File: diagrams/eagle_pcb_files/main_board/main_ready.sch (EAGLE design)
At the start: 32 parts

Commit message: prepare main board for production
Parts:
- C1, C2, C3, C4, C6, C7: value (none) -> 100nF
- FUSE1, FUSE2: value (none) -> 1.5A
- R1, R2: value (none) -> 10k
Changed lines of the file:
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@@
 <part name="RAO3" library="POLOLU-VoltageConverter" deviceset="S7V8F3" device=""/>
 <part name="BAT1" library="pinhead" deviceset="PINHD-1X2" device=""/>
-<part name="FUSE1" library="pinhead" deviceset="PINHD-1X2" device=""/>
+<part name="FUSE1" library="pinhead" deviceset="PINHD-1X2" device="" value="1.5A"/>
 <part name="RAO4" library="POLOLU-VoltageConverter" deviceset="S7V8F3" device=""/>
 <part name="BAT2" library="pinhead" deviceset="PINHD-1X2" device=""/>
-<part name="FUSE2" library="pinhead" deviceset="PINHD-1X2" device=""/>
+<part name="FUSE2" library="pinhead" deviceset="PINHD-1X2" device="" value="1.5A"/>
 <part name="U$3" library="SparFun-FuelGauge" deviceset="POLOLU_FUEL_GAUGE" device="BREAKBOARD"/>
 <part name="U$9" library="SparFun-FuelGauge" deviceset="POLOLU_FUEL_GAUGE" device="BREAKBOARD"/>
-<part name="C1" library="rcl" library_urn="urn:adsk.eagle:library:334" deviceset="C-EU" device="C0402" package3d_urn="urn:adsk.eagle:package:23626/1"/>
-<part name="C2" library="rcl" library_urn="urn:adsk.eagle:library:334" deviceset="C-EU" device="C0402" package3d_urn="urn:adsk.eagle:package:23626/1"/>
-<part name="C3" library="rcl" library_urn="urn:adsk.eagle:library:334" deviceset="C-EU" device="C0402" package3d_urn="urn:adsk.eagle:package:23626/1"/>
-<part name="C6" library="rcl" library_urn="urn:adsk.eagle:library:334" deviceset="C-EU" device="C0402" package3d_urn="urn:adsk.eagle:package:23626/1"/>
-<part name="C7" library="rcl" library_urn="urn:adsk.eagle:library:334" deviceset="C-EU" device="C0402" package3d_urn="urn:adsk.eagle:package:23626/1"/>
+<part name="C1" library="rcl" library_urn="urn:adsk.eagle:library:334" deviceset="C-EU" device="C0402" package3d_urn="urn:adsk.eagle:package:23626/1" value="100nF"/>
+<part name="C2" library="rcl" library_urn="urn:adsk.eagle:library:334" deviceset="C-EU" device="C0402" package3d_urn="urn:adsk.eagle:package:23626/1" value="100nF"/>
+<part name="C3" library="rcl" library_urn="urn:adsk.eagle:library:334" deviceset="C-EU" device="C0402" package3d_urn="urn:adsk.eagle:package:23626/1" value="100nF"/>
+<part name="C6" library="rcl" library_urn="urn:adsk.eagle:library:334" deviceset="C-EU" device="C0402" package3d_urn="urn:adsk.eagle:package:23626/1" value="100nF"/>
+<part name="C7" library="rcl" library_urn="urn:adsk.eagle:library:334" deviceset="C-EU" device="C0402" package3d_urn="urn:adsk.eagle:package:23626/1" value="100nF"/>
 <part name="GND2" library="supply1" library_urn="urn:adsk.eagle:library:371" deviceset="GND" device=""/>
 <part name="GND3" library="supply1" library_urn="urn:adsk.eagle:library:371" deviceset="GND" device=""/>
@@
 <part name="C9" library="rcl" library_urn="urn:adsk.eagle:library:334" deviceset="C-EU" device="C0402" package3d_urn="urn:adsk.eagle:package:23626/1" value="100 nF"/>
 <part name="GND5" library="supply1" library_urn="urn:adsk.eagle:library:371" deviceset="GND" device=""/>
-<part name="C4" library="rcl" library_urn="urn:adsk.eagle:library:334" deviceset="C-EU" device="C0402" package3d_urn="urn:adsk.eagle:package:23626/1"/>
+<part name="C4" library="rcl" library_urn="urn:adsk.eagle:library:334" deviceset="C-EU" device="C0402" package3d_urn="urn:adsk.eagle:package:23626/1" value="100nF"/>
 <part name="J3" library="Wurth_Elektronik_Electromechanic_FPC_Connectors_&amp;_Flat_Flexible_Cable_rev18c" library_urn="urn:adsk.eagle:library:488576" deviceset="686114183522" device="" package3d_urn="urn:adsk.eagle:package:3360859/1"/>
 <part name="U$1" library="BERRYIMU" deviceset="BERRYGPS-IMUV3" device="THROUGH_HOLE_ALPHA"/>
@@
 <part name="SHDN" library="testpad" library_urn="urn:adsk.eagle:library:385" deviceset="TP" device="TP19R" package3d_urn="urn:adsk.eagle:package:27972/1" value="TPTP19R"/>
 <part name="SHDN2" library="testpad" library_urn="urn:adsk.eagle:library:385" deviceset="TP" device="TP20R" package3d_urn="urn:adsk.eagle:package:27973/1" value="TPTP20R"/>
-<part name="R1" library="rcl" library_urn="urn:adsk.eagle:library:334" deviceset="R-EU_" device="M1206" package3d_urn="urn:adsk.eagle:package:23566/1"/>
-<part name="R2" library="rcl" library_urn="urn:adsk.eagle:library:334" deviceset="R-EU_" device="M1206" package3d_urn="urn:adsk.eagle:package:23566/1"/>
+<part name="R1" library="rcl" library_urn="urn:adsk.eagle:library:334" deviceset="R-EU_" device="M1206" package3d_urn="urn:adsk.eagle:package:23566/1" value="10k"/>
+<part name="R2" library="rcl" library_urn="urn:adsk.eagle:library:334" deviceset="R-EU_" device="M1206" package3d_urn="urn:adsk.eagle:package:23566/1" value="10k"/>
 <part name="C5" library="rcl" library_urn="urn:adsk.eagle:library:334" deviceset="C-EU" device="C0402" package3d_urn="urn:adsk.eagle:package:23626/1" value="100 nF"/>
+<part name="GND1" library="supply1" library_urn="urn:adsk.eagle:library:371" deviceset="GND" device=""/>
 </parts>
 <sheets>
@@
 <attribute name="NAME" x="-114.3" y="-23.749" size="1.778" layer="95" rot="R180"/>
 </instance>
+<instance part="GND1" gate="1" x="126.492" y="47.244" smashed="yes">
+<attribute name="VALUE" x="123.952" y="44.704" size="1.778" layer="96"/>
+</instance>
 </instances>
 <busses>
@@
 <pinref part="RAO2" gate="G$1" pin="GND@5"/>
 <wire x1="121.412" y1="67.31" x2="121.412" y2="54.61" width="0.1524" layer="91"/>
-<wire x1="121.412" y1="54.61" x2="121.412" y2="49.53" width="0.1524" layer="91"/>
 <wire x1="121.412" y1="67.31" x2="116.84" y2="67.31" width="0.1524" layer="91"/>
 <junction x="121.412" y="67.31"/>
@@
 <wire x1="121.412" y1="54.61" x2="116.84" y2="54.61" width="0.1524" layer="91"/>
 <junction x="121.412" y="54.61"/>
-<pinref part="RAO2" gate="G$1" pin="GND@7"/>
-<wire x1="121.412" y1="49.53" x2="116.84" y2="49.53" width="0.1524" layer="91"/>
 <pinref part="GND10" gate="1" pin="GND"/>
-<wire x1="121.412" y1="32.004" x2="121.412" y2="49.53" width="0.1524" layer="91"/>
+<wire x1="121.412" y1="32.004" x2="121.412" y2="54.61" width="0.1524" layer="91"/>
 </segment>
 <segment>
@@
 <wire x1="-143.002" y1="66.802" x2="-143.002" y2="85.09" width="0.1524" layer="91"/>
 <junction x="-143.002" y="85.09"/>
+</segment>
+<segment>
+<pinref part="GND1" gate="1" pin="GND"/>
+<pinref part="RAO2" gate="G$1" pin="GND@7"/>
+<wire x1="126.492" y1="49.784" x2="116.84" y2="49.784" width="0.1524" layer="91"/>
+<wire x1="116.84" y1="49.784" x2="116.84" y2="49.53" width="0.1524" layer="91"/>
 </segment>
 </net>
@@
 </sheet>
 </sheets>
+<errors>
+</errors>
 </schematic>
 </drawing>

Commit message: make board-schematic consistent
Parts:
- removed U$1: BERRYGPS-IMUV3THROUGH_HOLE_ALPHA, BERRYIMU:BERRYGPS-IMUV3THROUGH_HOLE_ALPHA
- C1, C10, C11, C2, C3, C4, C6, C7, C8, C9: device rcl:C-EUC0402 -> rcl:C-EUC0805
- C5: value 100 nF -> 100nF; device rcl:C-EUC0402 -> rcl:C-EUC0805
- R1, R2: value 10k -> 4.7k
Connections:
- removed net 3V3: RAO2.3V3@1, U$1.3V3
- removed net 5V0@1: RAO2.5V0@1, U$1.5V@1
- removed net 5V0@2: RAO2.5V0@2, U$1.5V@2
- removed net GND@3: RAO2.GND@1, RAO2.GND@3
- removed net RX: RAO2.RXD0/GPIO15, U$1.RXD
- removed net TX: RAO2.TXD0/GPIO14, U$1.TXD
- new net 5V: RAO2.5V0@1, RAO2.5V0@2
- net 3.3V: now also RAO2.3V3@1
- net A0: now also J3.3; no longer J3.2
- net A1: now also J3.2; no longer J3.3
- net B1: now also RAO2.GPIO13; no longer RAO2.GPIO5
- net B3: now also RAO2.GPIO5; no longer RAO2.GPIO13
- net DIO0: no longer U$1.GPIO4
- net GND: now also RAO2.GND@1, RAO2.GND@3, RAO2.GND@4; no longer U$1.GND@1, U$1.GND@2
- net SCL: no longer U$1.SCL
- net SDA: no longer U$1.SDA
- net VIN1: no longer J2.2, J3.1
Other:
- moved on the sheet: C5

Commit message: remove res from safetypin, fix fuel gauge circuit, add jumper to ommit fuel gauge
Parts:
- removed C11: 10 uF, rcl:C-EUC0805
- removed C9: 100 nF, rcl:C-EUC0805
- removed R1, R2: 4.7k, rcl:R-EU_M1206
- added C12: 100 nF, rcl:C-EUC0805
- added C13: 10uF, rcl:CPOL-EUSMCA
- added SJ1, SJ2: (no value), jumper:SJW
- C10: value 10 uF -> 10uF; device rcl:C-EUC0805 -> rcl:CPOL-EUSMCA
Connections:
- removed net SHDN: R2.1, RAO3.SHDN, SHDN.TP
- new net A: D1.C, RAO3.VIN
- new net B: D4.C, RAO4.VIN
- new net SHDN1: RAO3.SHDN, SHDN.TP
- net 3.3V: no longer C6.1, C7.1, U$3.VCC, U$9.VCC
- net BIN1: now also SJ1.1, U$3.+; no longer D1.A
- net BIN2: now also SJ2.1, U$9.+; no longer D4.A
- net GND: now also C10.-, C12.2, C13.-, C6.1; no longer C10.2, C11.1, C6.2, C9.1, R1.1, R2.2
- net SHDN2: no longer R1.2
- net VIN1: now also C7.1, D1.A, SJ1.2, U$3.VCC; no longer D1.C, RAO3.VIN, U$3.+
- net VIN2: now also C6.2, D4.A, J3.1, SJ2.2, U$9.VCC; no longer D4.C, RAO4.VIN, U$9.+
- net VOUT1: now also C10.+; no longer C10.1
- net VOUT2: now also C12.1, C13.+; no longer C11.2, C9.2
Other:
- moved on the sheet: C6, C7, C8, D1, D4, FUSE1, FUSE2, GND, SHDN, SHDN2

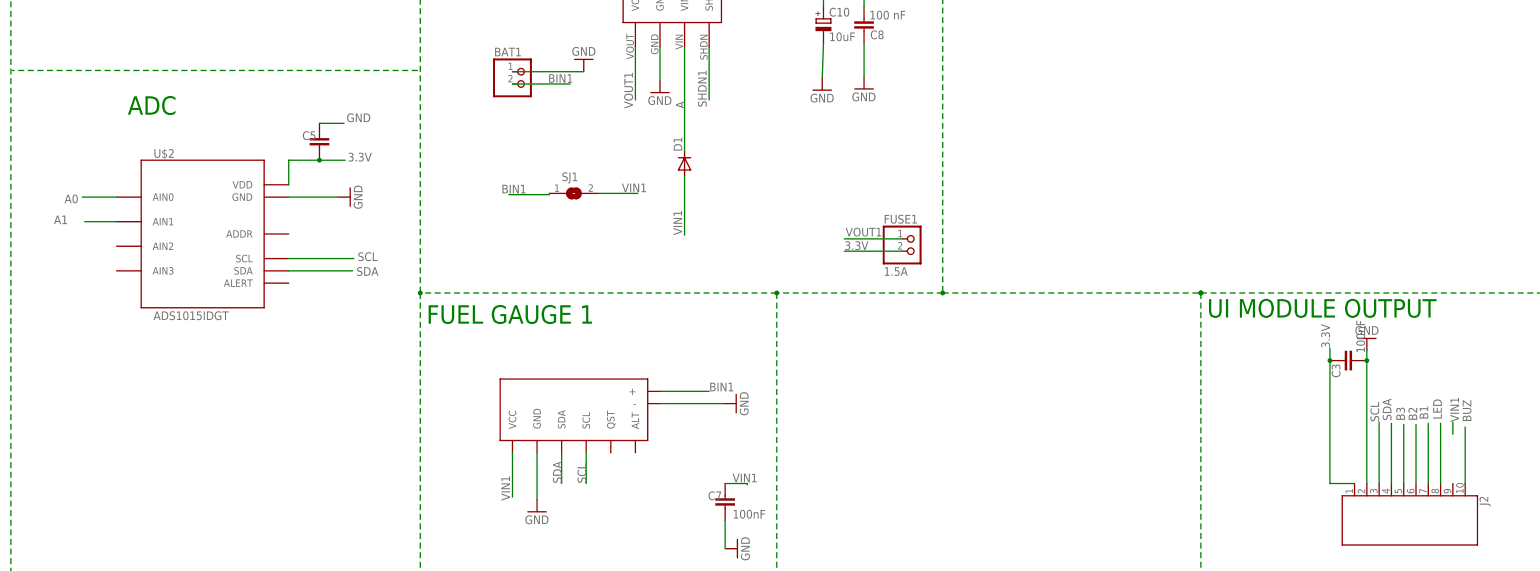
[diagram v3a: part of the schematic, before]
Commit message: remove adc from main board
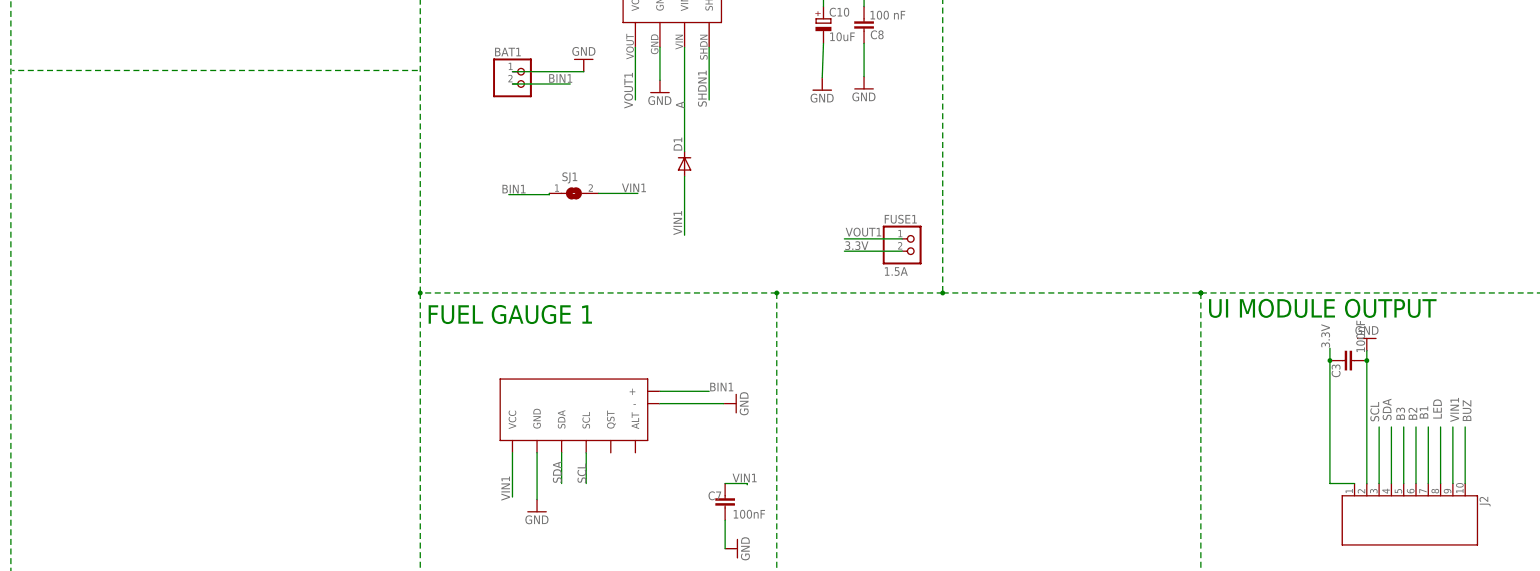
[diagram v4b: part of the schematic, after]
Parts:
- removed C5: 100nF, rcl:C-EUC0805
- removed U$2: ADS1015IDGT, bt_adc:ADS1015IDGT
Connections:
- net 3.3V: no longer C5.2, U$2.VDD
- net A0: no longer U$2.AIN0
- net A1: no longer U$2.AIN1
- net GND: no longer C5.1, U$2.GND
- net SCL: no longer U$2.SCL
- net SDA: no longer U$2.SDA
- net VIN1: now also J2.2
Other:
- note removed: "ADC"
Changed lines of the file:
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@@
 <part name="J3" library="Wurth_Elektronik_Electromechanic_FPC_Connectors_&amp;_Flat_Flexible_Cable_rev18c" library_urn="urn:adsk.eagle:library:488576" deviceset="686114183522" device="" package3d_urn="urn:adsk.eagle:package:3360859/1"/>
 <part name="J2" library="Wurth_Elektronik_Electromechanic_FPC_Connectors_&amp;_Flat_Flexible_Cable_rev18c" library_urn="urn:adsk.eagle:library:488576" deviceset="686110183522" device="" package3d_urn="urn:adsk.eagle:package:3360857/1"/>
-<part name="U$2" library="bt_adc" deviceset="ADS1015" device="IDGT"/>
-<part name="GND13" library="bt" deviceset="GND" device=""/>
 <part name="GND" library="testpad" library_urn="urn:adsk.eagle:library:385" deviceset="TP" device="TP19R" package3d_urn="urn:adsk.eagle:package:27972/1" value="TPTP19R"/>
 <part name="SHDN" library="testpad" library_urn="urn:adsk.eagle:library:385" deviceset="TP" device="TP19R" package3d_urn="urn:adsk.eagle:package:27972/1" value="TPTP19R"/>
 <part name="SHDN2" library="testpad" library_urn="urn:adsk.eagle:library:385" deviceset="TP" device="TP20R" package3d_urn="urn:adsk.eagle:package:27973/1" value="TPTP20R"/>
-<part name="C5" library="rcl" library_urn="urn:adsk.eagle:library:334" deviceset="C-EU" device="C0805" package3d_urn="urn:adsk.eagle:package:23617/2" value="100nF"/>
 <part name="C10" library="rcl" library_urn="urn:adsk.eagle:library:334" deviceset="CPOL-EU" device="SMCA" package3d_urn="urn:adsk.eagle:package:23431/1" value="10uF"/>
 <part name="GND1" library="supply1" library_urn="urn:adsk.eagle:library:371" deviceset="GND" device=""/>
@@
 <text x="-176.53" y="96.774" size="3.81" layer="91">SAFETY PIN 1</text>
 <text x="131.064" y="16.002" size="3.81" layer="91">BERRY-GPS IMU</text>
-<text x="-155.702" y="-10.16" size="3.81" layer="91">ADC</text>
 </plain>
 <instances>
@@
 <attribute name="VALUE" x="92.71" y="-88.9" size="1.778" layer="96" rot="R270"/>
 </instance>
-<instance part="U$2" gate="G$1" x="-140.208" y="-34.798" smashed="yes">
-<attribute name="NAME" x="-150.368" y="-19.05" size="1.778" layer="95"/>
-<attribute name="VALUE" x="-150.368" y="-52.578" size="1.778" layer="95"/>
-</instance>
-<instance part="GND13" gate="1" x="-109.728" y="-27.178" smashed="yes" rot="R90">
-<attribute name="VALUE" x="-107.188" y="-29.718" size="1.778" layer="96" rot="R90"/>
-</instance>
 <instance part="GND" gate="G$1" x="-144.272" y="78.994" smashed="yes" rot="R90">
 <attribute name="NAME" x="-145.288" y="78.994" size="1.778" layer="95" rot="R180"/>
@@
 <attribute name="NAME" x="-144.526" y="73.152" size="1.778" layer="95" rot="R180"/>
 <attribute name="TP_SIGNAL_NAME" x="-143.002" y="75.184" size="1.778" layer="97" rot="R90"/>
-</instance>
-<instance part="C5" gate="G$1" x="-116.078" y="-14.478" smashed="yes">
-<attribute name="NAME" x="-119.634" y="-15.367" size="1.778" layer="95"/>
 </instance>
 <instance part="C10" gate="G$1" x="-11.938" y="9.652" smashed="yes">
@@
 </segment>
 <segment>
-<pinref part="C5" gate="G$1" pin="1"/>
-<wire x1="-116.078" y1="-11.938" x2="-110.998" y2="-11.938" width="0.1524" layer="91"/>
-<label x="-110.49" y="-11.684" size="1.778" layer="95"/>
-</segment>
-<segment>
-<pinref part="GND13" gate="1" pin="GND"/>
-<pinref part="U$2" gate="G$1" pin="GND"/>
-<wire x1="-112.268" y1="-27.178" x2="-122.428" y2="-27.178" width="0.1524" layer="91"/>
-</segment>
-<segment>
 <pinref part="RAO3" gate="G$1" pin="GND"/>
 <pinref part="GND3" gate="1" pin="GND"/>
@@
 <net name="VIN1" class="0">
 <segment>
-<wire x1="118.11" y1="-76.2" x2="118.11" y2="-73.66" width="0.1524" layer="91"/>
+<wire x1="118.11" y1="-86.36" x2="118.11" y2="-74.676" width="0.1524" layer="91"/>
 <label x="119.38" y="-73.66" size="1.778" layer="95" rot="R90"/>
+<pinref part="J2" gate="G$1" pin="2"/>
 </segment>
 <segment>
@@
 <label x="58.674" y="90.424" size="1.778" layer="95"/>
 </segment>
-<segment>
-<pinref part="C5" gate="G$1" pin="2"/>
-<wire x1="-116.078" y1="-19.558" x2="-110.744" y2="-19.558" width="0.1524" layer="91"/>
-<label x="-110.236" y="-19.812" size="1.778" layer="95"/>
-<pinref part="U$2" gate="G$1" pin="VDD"/>
-<wire x1="-122.428" y1="-24.638" x2="-122.428" y2="-19.558" width="0.1524" layer="91"/>
-<wire x1="-122.428" y1="-19.558" x2="-116.078" y2="-19.558" width="0.1524" layer="91"/>
-<junction x="-116.078" y="-19.558"/>
-</segment>
 </net>
 <net name="VOUT1" class="0">
@@
 </segment>
 <segment>
-<wire x1="102.87" y1="-86.36" x2="102.87" y2="-73.66" width="0.1524" layer="91"/>
+<wire x1="102.87" y1="-86.36" x2="102.87" y2="-74.676" width="0.1524" layer="91"/>
 <label x="102.87" y="-73.66" size="1.778" layer="95" rot="R90"/>
 <pinref part="J2" gate="G$1" pin="8"/>
@@
 <label x="234.442" y="-26.416" size="1.778" layer="95"/>
 </segment>
-<segment>
-<pinref part="U$2" gate="G$1" pin="SCL"/>
-<wire x1="-122.428" y1="-39.878" x2="-108.966" y2="-39.878" width="0.1524" layer="91"/>
-<label x="-108.204" y="-40.386" size="1.778" layer="95"/>
-</segment>
 </net>
 <net name="SDA" class="0">
@@
 <segment>
 <label x="105.41" y="-73.406" size="1.778" layer="95" rot="R90"/>
-<wire x1="105.41" y1="-73.914" x2="105.41" y2="-86.36" width="0.1524" layer="91"/>
+<wire x1="105.41" y1="-74.676" x2="105.41" y2="-86.36" width="0.1524" layer="91"/>
 <pinref part="J2" gate="G$1" pin="7"/>
 </segment>
@@
 <label x="234.188" y="-23.876" size="1.778" layer="95"/>
 </segment>
-<segment>
-<pinref part="U$2" gate="G$1" pin="SDA"/>
-<wire x1="-122.428" y1="-42.418" x2="-109.22" y2="-42.418" width="0.1524" layer="91"/>
-<label x="-108.458" y="-43.434" size="1.778" layer="95"/>
-</segment>
 </net>
 <net name="B1" class="0">
 <segment>
 <label x="113.03" y="-73.152" size="1.778" layer="95" rot="R90"/>
-<wire x1="113.03" y1="-86.36" x2="113.03" y2="-73.914" width="0.1524" layer="91"/>
+<wire x1="113.03" y1="-86.36" x2="113.03" y2="-74.676" width="0.1524" layer="91"/>
 <pinref part="J2" gate="G$1" pin="4"/>
 </segment>
@@
 <segment>
 <label x="110.744" y="-73.406" size="1.778" layer="95" rot="R90"/>
-<wire x1="110.49" y1="-74.168" x2="110.49" y2="-86.36" width="0.1524" layer="91"/>
+<wire x1="110.49" y1="-74.676" x2="110.49" y2="-86.36" width="0.1524" layer="91"/>
 <pinref part="J2" gate="G$1" pin="5"/>
 </segment>
@@
 <segment>
 <label x="108.204" y="-73.406" size="1.778" layer="95" rot="R90"/>
-<wire x1="107.95" y1="-86.36" x2="107.95" y2="-74.168" width="0.1524" layer="91"/>
+<wire x1="107.95" y1="-86.36" x2="107.95" y2="-74.676" width="0.1524" layer="91"/>
 <pinref part="J2" gate="G$1" pin="6"/>
 </segment>
@@
 <segment>
 <pinref part="J2" gate="G$1" pin="3"/>
-<wire x1="115.57" y1="-86.36" x2="115.57" y2="-73.914" width="0.1524" layer="91"/>
+<wire x1="115.57" y1="-86.36" x2="115.57" y2="-74.676" width="0.1524" layer="91"/>
 <label x="115.824" y="-73.152" size="1.778" layer="95" rot="R90"/>
 </segment>
@@
 <net name="A0" class="0">
 <segment>
-<pinref part="U$2" gate="G$1" pin="AIN0"/>
-<wire x1="-157.988" y1="-27.178" x2="-165.1" y2="-27.178" width="0.1524" layer="91"/>
-<label x="-165.862" y="-26.67" size="1.778" layer="95" rot="R180"/>
-</segment>
-<segment>
 <pinref part="J3" gate="G$1" pin="3"/>
 <wire x1="251.46" y1="-2.54" x2="239.776" y2="-2.54" width="0.1524" layer="91"/>
@@
 <net name="A1" class="0">
 <segment>
-<pinref part="U$2" gate="G$1" pin="AIN1"/>
-<wire x1="-157.988" y1="-32.258" x2="-164.592" y2="-32.258" width="0.1524" layer="91"/>
-<label x="-170.942" y="-32.766" size="1.778" layer="95"/>
-</segment>
-<segment>
 <pinref part="J3" gate="G$1" pin="2"/>
